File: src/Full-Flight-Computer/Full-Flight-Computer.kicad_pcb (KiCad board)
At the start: 4 copper layers, 93.7 x 43.7 mm, 113 parts, among them J1 Jumper_NO, J2 Jumper_NO, P1 647676-2, P10 Micro_SD_Card, P2 1546551-2, P3 3220-20-0200-00, P4 440054-3, P5 440054-3, P6 440054-3, P7 440054-3, P8 USB, P9 1984659, Q1 QS5U17TR, Q2 QS5U17TR, Q3 QS5U17TR, Q4 QS5U17TR, Q5 QS5U17TR, Q6 QS5U17TR, U1 STM32H750VBTx, U10 TS391IYLT, U11 TS391IYLT, U12 BMM150, U2 LMS8117AMP-3.3_NOPB, U3 BMI323, U4 MAX-8C-0-10, U5 BMP390, U6 SST25VF040B-50-4I-S2AE-T, U7 RFM95W-868S2, U8 CP2102-GMR(QFN28), U9 TS391IYLT, Y1 ECS-240-18-33-JGN-TR

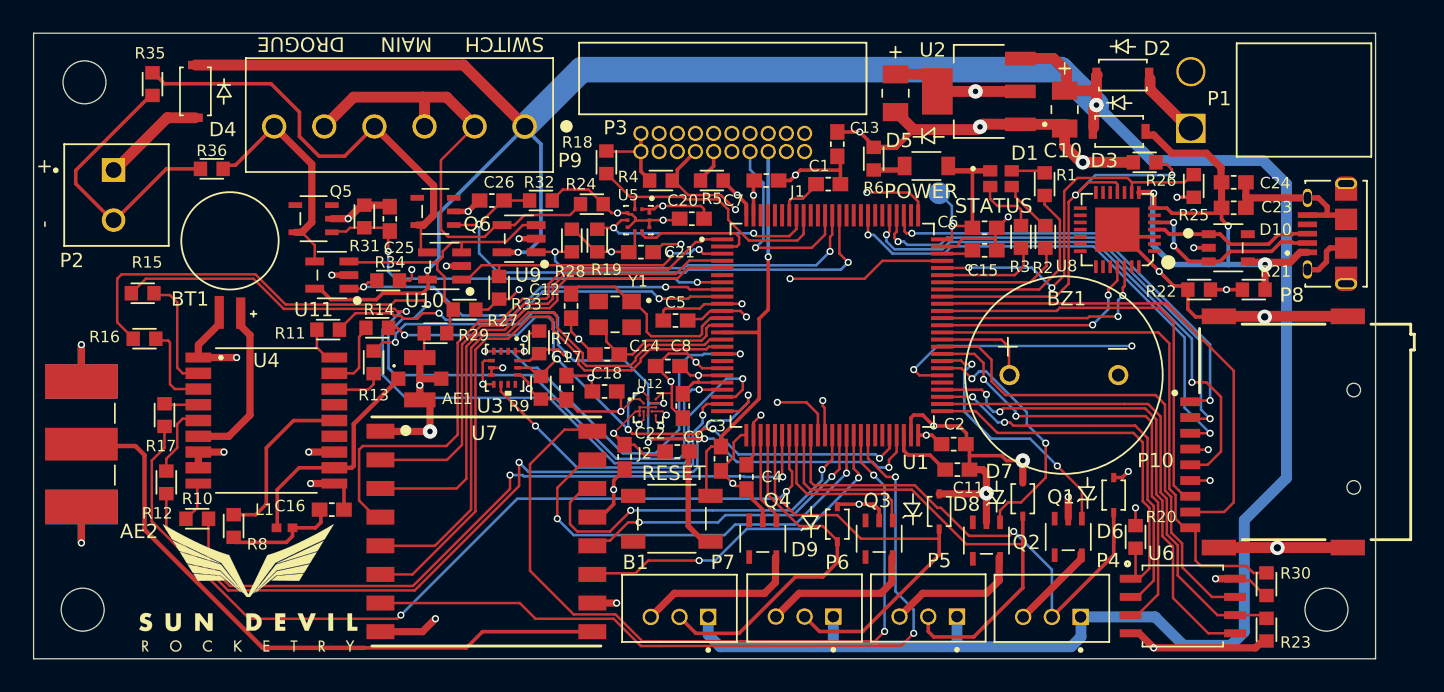
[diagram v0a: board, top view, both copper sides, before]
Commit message: placed all components on test board
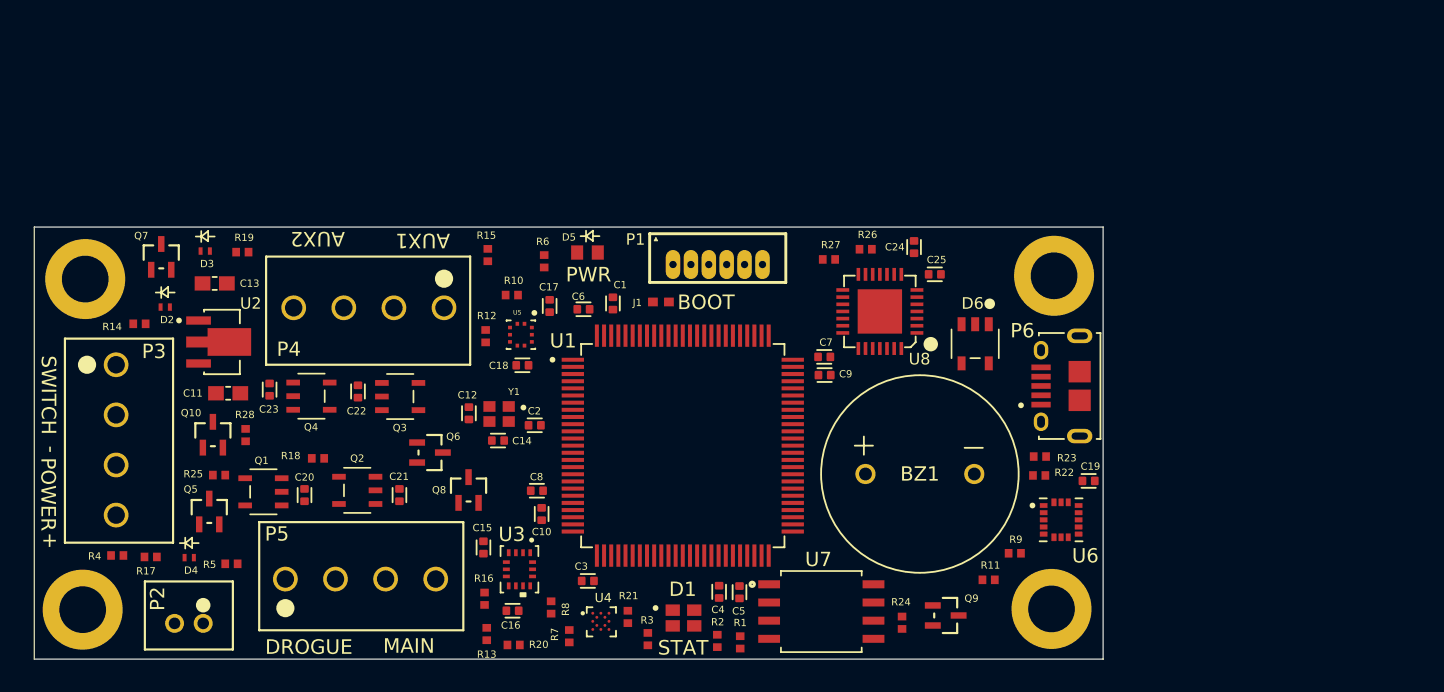
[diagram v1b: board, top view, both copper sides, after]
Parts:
- removed AE1: 0734120110, Flight-Computer:73412-0110
- removed AE2: 142-0701-851, Flight-Computer:142-0701-851
- removed B1: PTS647SM38SMTR2LFS, Flight-Computer:PTS647SM38SMTR2LFS
- removed BT1: MS614SE-FL28E, Flight-Computer:MS621FE-FL11E
- removed the C10 at (165.0, 63.2)
- removed the C16 at (113.8, 91.2)
- removed the C25 at (117.8, 70.9)
- removed C26: 1uF, Flight-Computer:CAP_0603
- removed the C3 at (141.0, 87.6)
- removed the D6 at (168.4, 90.2)
- removed D7, D8, D9: MM3Z3V3B, Flight-Computer:MM3Z3V3B
- removed the H3 at (183.3, 98.2)
- removed J2: Jumper_NO, Engine-Controller:Jumper-NO
- removed L1: 27nH, Flight-Computer:L-07C27NJV6T
- removed LOGO1: Logo, Flight-Computer:Logo
- removed P10: Micro_SD_Card, Flight-Computer:MEM2075-00-140-01-A
- removed the P6 at (148.8, 98.7)
- removed P7: 440054-3, Flight-Computer:440054-3
- removed P9: 1984659, Flight-Computer:1984659
- removed the R10 at (104.4, 91.8)
- removed the R12 at (102.2, 89.3)
- removed the R24 at (132.0, 69.8)
- removed the R27 at (123.1, 77.2)
- removed R29, R30, R33, R34, R35, R36: 10k, Flight-Computer:RES_0603
- removed R31, R32: 100k, Flight-Computer:RES_0603
- removed the R8 at (106.9, 92.3)
- removed TP1: TP, Flight-Computer:TP
- removed U10, U11, U9: TS391IYLT, Flight-Computer:TS391IYLT
- removed the U4 at (109.2, 85.0)
- removed the U7 at (124.6, 92.7)
- added C11: 1uF, Full-Flight-Computer:CAP_0603, F.Cu at (106.6, 83.1)
- added C19: 0.1uF, Full-Flight-Computer:CAP_0402, F.Cu at (166.6, 89.2)
- added C20: 1uF, Full-Flight-Computer:CAP_0402, F.Cu at (111.9, 90.2)
- added C21: 1uF, Full-Flight-Computer:CAP_0402, F.Cu at (118.5, 90.2)
- added C23: 1uF, Full-Flight-Computer:CAP_0402, F.Cu at (109.4, 82.8)
- added H2: Mounting-Hole-4-40, Full-Flight-Computer:MountingHole_4-40, F.Cu at (164.2, 74.9)
- added H4: Mounting-Hole, Full-Flight-Computer:MountingHole_4-40, F.Cu at (96.6, 75.1)
- added Q10: 2N7002W-7-F, Full-Flight-Computer:2N7002W-7-F, F.Cu at (105.5, 86.0)
- added Q7: 2N7002W-7-F, Full-Flight-Computer:2N7002W-7-F, F.Cu at (101.9, 73.5)
- added Q8: 2N7002W-7-F, Full-Flight-Computer:2N7002W-7-F, F.Cu at (123.3, 89.8)
- added Q9: 2N7002W-7-F, Full-Flight-Computer:2N7002W-7-F, F.Cu at (156.7, 98.6)
- added R18: 10k, Full-Flight-Computer:RES_0402, F.Cu at (112.8, 87.6)
- added R19: 10k, Full-Flight-Computer:RES_0402, F.Cu at (107.5, 73.2)
- added R20: 10k, Full-Flight-Computer:RES_0402, F.Cu at (126.5, 100.6)
- added R25: 100k, Full-Flight-Computer:RES_0402, F.Cu at (105.9, 88.8)
- added R9: 10k, Full-Flight-Computer:RES_0402, F.Cu at (161.5, 94.2)
- added U6: H3LIS100DLTR, Full-Flight-Computer:H3LIS100DLTR, F.Cu at (164.7, 91.9)
- BZ1: footprint Flight-Computer:AT-1438-TWT-R -> Full-Flight-Computer:AT-1438-TWT-R
- C1, C12, C14, C2, C5, C6, C7, C8: footprint Flight-Computer:CAP_0603 -> Full-Flight-Computer:CAP_0402
- C10: renamed from C9; footprint Flight-Computer:CAP_0603 -> Full-Flight-Computer:CAP_0402
- C13: value 10uF -> 1uF; footprint Flight-Computer:T491A106K010AT -> Full-Flight-Computer:CAP_0603
- C15: renamed from C17; footprint Flight-Computer:CAP_0603 -> Full-Flight-Computer:CAP_0402
- C16: renamed from C18; footprint Flight-Computer:CAP_0603 -> Full-Flight-Computer:CAP_0402
- C17: renamed from C20; footprint Flight-Computer:CAP_0603 -> Full-Flight-Computer:CAP_0402
- C18: renamed from C21; footprint Flight-Computer:CAP_0603 -> Full-Flight-Computer:CAP_0402
- C22: value 0.1uF -> 1uF; footprint Flight-Computer:CAP_0603 -> Full-Flight-Computer:CAP_0402
- C24: renamed from C23; footprint Flight-Computer:CAP_0603 -> Full-Flight-Computer:CAP_0402
- C25: renamed from C24; footprint Flight-Computer:CAP_0603 -> Full-Flight-Computer:CAP_0402
- C3: renamed from C4; footprint Flight-Computer:CAP_0603 -> Full-Flight-Computer:CAP_0402
- C4: renamed from C11; footprint Flight-Computer:CAP_0603 -> Full-Flight-Computer:CAP_0402
- C9: renamed from C15; footprint Flight-Computer:CAP_0603 -> Full-Flight-Computer:CAP_0402
- D1: footprint Flight-Computer:CLMVC-FKA-CL1D1L71BB7C3C3 -> Full-Flight-Computer:CLMVC-FKA-CL1D1L71BB7C3C3
- D2, D3, D4: value SM5819PL-TP -> PMEG3010AESBYL; footprint Flight-Computer:SM5819PL-TP -> Full-Flight-Computer:PMEG3010AESBYL
- D5: value SML-LX1206GC-TR -> LTST-C191KGKT; footprint Flight-Computer:SML-LX1206GC-TR -> Full-Flight-Computer:LTST-C191KGKT
- D6: renamed from D10; footprint Flight-Computer:SP0504BAHTG -> Full-Flight-Computer:SP0504BAHTG
- H1: value Mounting-Hole -> Mounting-Hole-4-40; footprint Flight-Computer:MountingHole_3mm -> Full-Flight-Computer:MountingHole_4-40
- H3: renamed from H2; footprint Flight-Computer:MountingHole_3mm -> Full-Flight-Computer:MountingHole_4-40
- J1: footprint Flight-Computer:Jumper-NO -> Full-Flight-Computer:Jumper-NO
- P1: value 647676-2 -> 0530470610; footprint Flight-Computer:647676-2 -> Full-Flight-Computer:53047-0610
- P2: value 1546551-2 -> B2B-PH-K-SLFSN_JST; footprint Flight-Computer:1546551-2 -> Full-Flight-Computer:B2B-PH-K-SLFSN_JST
- P3: value 3220-20-0200-00 -> 1984659; footprint Flight-Computer:3220-20-0200-00 -> Full-Flight-Computer:1546551-4
- P4: value 440054-3 -> 1546551-4; footprint Flight-Computer:440054-3 -> Full-Flight-Computer:1546551-4
- P5: value 440054-3 -> 1984659; footprint Flight-Computer:440054-3 -> Full-Flight-Computer:1546551-4
- P6: renamed from P8; footprint Flight-Computer:10118194-0001LF -> Full-Flight-Computer:10118194-0001LF
- Q1, Q2, Q3, Q4: footprint Flight-Computer:QS5U17TR -> Full-Flight-Computer:QS5U17TR
- Q5, Q6: value QS5U17TR -> 2N7002W-7-F; footprint Flight-Computer:QS5U17TR -> Full-Flight-Computer:2N7002W-7-F
- R1: value 68 -> 82; footprint Flight-Computer:RES_0603 -> Full-Flight-Computer:RES_0402
- R10: renamed from R18; footprint Flight-Computer:RES_0603 -> Full-Flight-Computer:RES_0402
- R11, R17: value 33 -> 10k; footprint Flight-Computer:RES_0603 -> Full-Flight-Computer:RES_0402
- R12: renamed from R19; footprint Flight-Computer:RES_0603 -> Full-Flight-Computer:RES_0402
- R13, R14, R15, R16: value 33 -> 100k; footprint Flight-Computer:RES_0603 -> Full-Flight-Computer:RES_0402
- R2, R28, R6: footprint Flight-Computer:RES_0603 -> Full-Flight-Computer:RES_0402
- R21: renamed from R20; footprint Flight-Computer:RES_0603 -> Full-Flight-Computer:RES_0402
- R22: renamed from R21; value 10k -> 100k; footprint Flight-Computer:RES_0603 -> Full-Flight-Computer:RES_0402
- R23: renamed from R22; value 20k -> 200k; footprint Flight-Computer:RES_0603 -> Full-Flight-Computer:RES_0402
- R24: renamed from R23; footprint Flight-Computer:RES_0603 -> Full-Flight-Computer:RES_0402
- R26: renamed from R25; footprint Flight-Computer:RES_0603 -> Full-Flight-Computer:RES_0402
- R27: renamed from R26; footprint Flight-Computer:RES_0603 -> Full-Flight-Computer:RES_0402
- R3: value 280 -> 240; footprint Flight-Computer:RES_0603 -> Full-Flight-Computer:RES_0402
- R4: value 100k -> 39k; footprint Flight-Computer:RES_0603 -> Full-Flight-Computer:RES_0402
- R5: value 100k -> 10k; footprint Flight-Computer:RES_0603 -> Full-Flight-Computer:RES_0402
- R7: footprint Engine-Controller:RES_0603 -> Full-Flight-Computer:RES_0402
- R8: renamed from R9; footprint Engine-Controller:RES_0603 -> Full-Flight-Computer:RES_0402
- U1: footprint Flight-Computer:STM32H750VBT6 -> Full-Flight-Computer:STM32H750VBT6
- U2: value LMS8117AMP-3.3_NOPB -> AP7370-33Y-13; footprint Flight-Computer:LMS8117AMP-3.3NOPB -> Full-Flight-Computer:AP7370-33Y-13
- U3: footprint Flight-Computer:BMI323 -> Full-Flight-Computer:BMI323
- U4: renamed from U12; footprint Flight-Computer:BMM150 -> Full-Flight-Computer:BMM150
- U5: footprint Flight-Computer:BMP390 -> Full-Flight-Computer:BMP390
- U7: renamed from U6; footprint Flight-Computer:SST25VF040B-50-4I-S2AE-T -> Full-Flight-Computer:SST25VF040B-50-4I-S2AE-T
- U8: footprint Flight-Computer:CP2012-GMR -> Full-Flight-Computer:CP2012-GMR
- Y1: footprint Flight-Computer:ECS-240-18-33-JGN-TR -> Full-Flight-Computer:ECS-240-12-37B-CKY-TR
- moved H1 76.9 mm to (164.1, 98.1)
- moved D2 68.8 mm to (102.2, 77.0)
- moved D3 64.4 mm to (105.0, 73.1)
- moved Q1 56.3 mm to (109.0, 89.9), turned to 180 degrees
- moved U2 55.7 mm to (106.1, 79.5), turned to 0 degrees
- moved P4 49.4 mm to (121.6, 77.1)
- moved C13 49.4 mm to (105.6, 75.4), turned to 0 degrees
- moved R11 49.3 mm to (159.7, 96.1), turned to 0 degrees
- moved P5 47.0 mm to (110.5, 96.0), turned to 0 degrees
- moved R4 46.1 mm to (98.8, 94.4), turned to 0 degrees
- moved P3 45.3 mm to (98.7, 81.1), turned to -90 degrees
- moved Q2 44.1 mm to (115.6, 89.8), turned to 180 degrees
- moved R5 42.9 mm to (106.8, 95.0)
- moved R1 38.4 mm to (142.3, 100.5)
- moved R3 38.3 mm to (135.9, 100.2), turned to -90 degrees
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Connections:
- BZ1 pad 1: BEEP -> VIN
- BZ1 pad 2: Earth -> Net-(BZ1-+)
- C22 pad 1: 3.3V -> AUX1
- P1 pad 1: /PIN_HARN -> 3.3V
- P1 pad 2: Earth -> SWDIO
- P2 pad 1: /PIN_SCREW -> Earth
- P2 pad 2: Earth -> Net-(P2-6)
- P3 pad 1: 3.3V -> VIN
- P3 pad 2: 3.3V -> VIN_SW
- P3 pad 4: Earth -> Net-(P3B-6)
- P4 pad 1: VIN -> VIN_SW
- P4 pad 2: MOTOR1_PWM -> Net-(P4A-6)
- P4 pad 3: Net-(P4-Pad3) -> VIN_SW
- P5 pad 1: VIN -> VIN_SW
- P5 pad 2: MOTOR3_PWM -> Net-(P5A-6)
- P5 pad 3: Net-(P5-Pad3) -> VIN_SW
- Q1 pad 1: MOTOR1_EN -> DROGUE
- Q1 pad 5: Net-(P4-Pad3) -> Net-(P5A-6)
- Q2 pad 1: MOTOR3_EN -> MAIN
- Q2 pad 5: Net-(P5-Pad3) -> Net-(P5B-6)
- Q3 pad 1: MOTOR2_EN -> AUX1
- Q3 pad 5: Net-(P6-Pad3) -> Net-(P4A-6)
- Q4 pad 1: MOTOR4_EN -> AUX2
- Q4 pad 5: Net-(P7-Pad3) -> Net-(P4B-6)
- Q5 pad 1: DROGUE -> Net-(P5B-6)
- Q5 pad 3: unconnected-(Q5-Pad3) -> ~{MAIN_CONT}
- Q6 pad 1: MAIN -> Net-(P4A-6)
- Q6 pad 3: unconnected-(Q6-Pad3) -> ~{AUX1_CONT}
- R11 pad 1: ~{GPS_SBOOT} -> HG_ACC_SDA
- R11 pad 2: Net-(R11-Pad2) -> 3.3V
- R13 pad 1: SDA -> Earth
- R13 pad 2: Net-(R13-Pad2) -> Net-(P5B-6)
- R14 pad 1: SCL -> Earth
- R14 pad 2: Net-(R14-Pad2) -> Net-(P4A-6)
- R15 pad 1: Net-(R15-Pad1) -> Earth
- R15 pad 2: GPS_TX -> Net-(P4B-6)
- R16 pad 1: Net-(R16-Pad1) -> Earth
- R16 pad 2: GPS_RX -> Net-(P5A-6)
- R17 pad 1: Net-(R17-Pad1) -> ~{MAIN_CONT}
- R17 pad 2: GPS_TIM -> 3.3V
- R4 pad 1: SWDIO -> VIN
- R4 pad 2: 3.3V -> VBAT_SENSE
- R5 pad 1: SWCLK -> Earth
- R5 pad 2: 3.3V -> VBAT_SENSE
- U1 pad 1: W_SCK -> unconnected-(U1-PE2-Pad1)
- U1 pad 15: W_SS -> unconnected-(U1-PC0-Pad15)
- U1 pad 16: W_RST -> unconnected-(U1-PC1-Pad16)
- U1 pad 22: GPS_RX -> unconnected-(U1-PA0-Pad22)
- U1 pad 23: GPS_TX -> unconnected-(U1-PA1-Pad23)
- U1 pad 25: GPS_INT -> unconnected-(U1-PA3-Pad25)
- U1 pad 28: MOTOR4_EN -> unconnected-(U1-PA4-Pad28)
- U1 pad 29: MOTOR4_PWM -> unconnected-(U1-PA5-Pad29)
- U1 pad 30: MOTOR2_PWM -> VBAT_SENSE
- U1 pad 31: ~{GPS_RST} -> unconnected-(U1-PA7-Pad31)
- U1 pad 32: GPS_TIM -> unconnected-(U1-PC4-Pad32)
- U1 pad 33: MOTOR2_EN -> unconnected-(U1-PC5-Pad33)
- U1 pad 34: MOTOR3_PWM -> HG_ACC_INT1
- U1 pad 35: MOTOR1_PWM -> HG_ACC_INT2
- U1 pad 38: W_IO0 -> unconnected-(U1-PE8-Pad38)
- U1 pad 39: W_IO4 -> unconnected-(U1-PE9-Pad39)
- U1 pad 4: W_MISO -> unconnected-(U1-PE5-Pad4)
- U1 pad 40: W_IO1 -> unconnected-(U1-PE10-Pad40)
- U1 pad 41: W_IO3 -> unconnected-(U1-PE11-Pad41)
- U1 pad 42: W_IO2 -> AUX1
- U1 pad 43: W_IO5 -> AUX2
- U1 pad 44: unconnected-(U1-Pad44) -> ~{AUX1_CONT}
- U1 pad 45: unconnected-(U1-Pad45) -> ~{AUX2_CONT}
- U1 pad 5: W_MOSI -> unconnected-(U1-PE6-Pad5)
- U1 pad 57: MOTOR3_EN -> unconnected-(U1-PD10-Pad57)
- U1 pad 58: MOTOR1_EN -> unconnected-(U1-PD11-Pad58)
- U1 pad 62: ~{SD_DETECT} -> unconnected-(U1-PD15-Pad62)
- U1 pad 65: SD_DAT0 -> unconnected-(U1-PC8-Pad65)
- U1 pad 66: SD_DAT1 -> unconnected-(U1-PC9-Pad66)
- U1 pad 78: SD_DAT2 -> unconnected-(U1-PC10-Pad78)
- U1 pad 79: SD_DAT3 -> unconnected-(U1-PC11-Pad79)
- U1 pad 80: SD_CLK -> unconnected-(U1-PC12-Pad80)
- U1 pad 83: SD_CMD -> unconnected-(U1-PD2-Pad83)
- U1 pad 9: ~{GPS_SBOOT} -> unconnected-(U1-PC15-Pad9)
- U1 pad 95: unconnected-(U1-Pad95) -> HG_ACC_SCL
- U1 pad 96: unconnected-(U1-Pad96) -> HG_ACC_SDA
- U2 pad 1: Earth -> 3.3V
- U2 pad 2: 3.3V -> Earth
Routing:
- net Earth: track 236.5 -> 0.00 mm, vias 43 -> 0
- net VIN: track 206.8 -> 0.00 mm, vias 3 -> 0
- net 3.3V: track 94.3 -> 0.00 mm, vias 23 -> 0
- net GPS_RX: track 64.1 -> 0.00 mm, vias 2 -> 0
- net GPS_TIM: track 62.0 -> 0.00 mm, vias 2 -> 0
- net GPS_TX: track 60.2 -> 0.00 mm, vias 2 -> 0
- net GPS_INT: track 56.3 -> 0.00 mm, vias 2 -> 0
- net W_IO5: track 54.4 -> 0.00 mm, vias 2 -> 0
- net W_IO2: track 54.2 -> 0.00 mm, vias 2 -> 0
- net SDA: track 53.1 -> 0.00 mm, vias 6 -> 0
- net ~{GPS_RST}: track 50.7 -> 0.00 mm, vias 2 -> 0
- net SCL: track 49.8 -> 0.00 mm, vias 6 -> 0
- net Net-(AE2-Pad1): track 43.2 -> 0.00 mm
- net W_SCK: track 41.2 -> 0.00 mm
- net W_RST: track 41.1 -> 0.00 mm
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- removed copper zone on In2.Cu, net 3.3V
- removed copper zone on In1.Cu, net Earth
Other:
- board size 93.7 x 43.7 mm -> 74.7 x 30.2 mm
- board text added: "A0002 Rev 2.0 Full-Feature Flight Computer Test Board"
- board text added: "AUX1"
- board text added: "AUX2"
- board text added: "BOOT"
- board text added: "PWR"
- board text added: "STAT"
- board text removed: "A0002 Flight Computer Rev 2.0"
- board text removed: "RESET"
- board text removed: "STATUS"

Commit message: completed initial layout
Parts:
- moved R4 64.7 mm to (159.7, 72.4), turned to 180 degrees
- moved D3 55.1 mm to (160.0, 75.3)
- moved R5 55.1 mm to (157.0, 72.4)
- moved R20 28.7 mm to (98.5, 94.4)
- moved R16 23.7 mm to (100.9, 94.6), turned to 0 degrees
- moved R17 21.4 mm to (122.3, 91.0)
- moved R21 20.9 mm to (155.3, 99.0)
- moved Q5 19.9 mm to (125.1, 91.7)
- moved Q8 18.4 mm to (105.0, 91.7), turned to 90 degrees
- moved D2 18.2 mm to (107.3, 94.5)
- moved R15 18.1 mm to (106.6, 73.4), turned to 0 degrees
- moved R14 16.9 mm to (115.6, 85.5), turned to 180 degrees
- moved R18 9.31 mm to (121.6, 84.4), turned to 90 degrees
- moved R19 7.43 mm to (101.2, 77.1)
- moved R7 5.80 mm to (129.3, 94.3), turned to 0 degrees
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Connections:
- U1 pad 15: unconnected-(U1-PC0-Pad15) -> ~{AUX1_CONT}
- U1 pad 16: unconnected-(U1-PC1-Pad16) -> MAIN
- U1 pad 17: IMU_INT1 -> DROGUE
- U1 pad 18: unconnected-(U1-PC3_C-Pad18) -> ~{DROGUE_CONT}
- U1 pad 22: unconnected-(U1-PA0-Pad22) -> ~{MAIN_CONT}
- U1 pad 24: IMU_INT2 -> IMU_INT1
- U1 pad 25: unconnected-(U1-PA3-Pad25) -> IMU_INT2
- U1 pad 3: ~{MAIN_CONT} -> unconnected-(U1-PE4-Pad3)
- U1 pad 31: unconnected-(U1-PA7-Pad31) -> MAG_DRDY
- U1 pad 32: unconnected-(U1-PC4-Pad32) -> MAG_INT
- U1 pad 34: HG_ACC_INT1 -> unconnected-(U1-PB0-Pad34)
- U1 pad 35: HG_ACC_INT2 -> unconnected-(U1-PB1-Pad35)
- U1 pad 36: MAG_DRDY -> unconnected-(U1-PB2-Pad36)
- U1 pad 37: MAG_INT -> unconnected-(U1-PE7-Pad37)
- U1 pad 39: unconnected-(U1-PE9-Pad39) -> STATUS_R
- U1 pad 41: unconnected-(U1-PE11-Pad41) -> STATUS_B
- U1 pad 42: AUX1 -> unconnected-(U1-PE12-Pad42)
- U1 pad 43: AUX2 -> STATUS_G
- U1 pad 44: ~{AUX1_CONT} -> unconnected-(U1-PE14-Pad44)
- U1 pad 45: ~{AUX2_CONT} -> unconnected-(U1-PE15-Pad45)
- U1 pad 5: unconnected-(U1-PE6-Pad5) -> ~{AUX2_CONT}
- U1 pad 55: unconnected-(U1-PD8-Pad55) -> HG_ACC_INT1
- U1 pad 56: USB_DETECT -> HG_ACC_INT2
- U1 pad 57: unconnected-(U1-PD10-Pad57) -> USB_DETECT
- U1 pad 68: STATUS_B -> unconnected-(U1-PA9-Pad68)
- U1 pad 69: STATUS_G -> unconnected-(U1-PA10-Pad69)
- U1 pad 7: DROGUE -> AUX2
- U1 pad 70: STATUS_R -> unconnected-(U1-PA11-Pad70)
- U1 pad 8: ~{DROGUE_CONT} -> AUX1
- U1 pad 87: MAIN -> unconnected-(U1-PD6-Pad87)
- U1 pad 88: ~{SWITCH} -> unconnected-(U1-PD7-Pad88)
- U1 pad 9: unconnected-(U1-PC15-Pad9) -> ~{SWITCH}
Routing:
- net Earth: track 0.00 -> 140.1 mm, vias 0 -> 33
- net VIN: track 0.00 -> 123.9 mm, vias 0 -> 3
- net 3.3V: track 0.00 -> 102.7 mm, vias 0 -> 22
- net VIN_SW: track 0.00 -> 67.4 mm
- net VBAT_SENSE: track 0.00 -> 47.2 mm, vias 0 -> 2
- net HG_ACC_SCL: track 0.00 -> 46.8 mm, vias 0 -> 3
- net ~{DROGUE_CONT}: track 0.00 -> 42.4 mm
- net ~{AUX2_CONT}: track 0.00 -> 41.6 mm, vias 0 -> 2
- net HG_ACC_SDA: track 0.00 -> 39.8 mm, vias 0 -> 2
- net 5V: track 0.00 -> 37.1 mm, vias 0 -> 1
- net SDA: track 0.00 -> 32.6 mm, vias 0 -> 2
- net AUX2: track 0.00 -> 31.9 mm
- net ~{SWITCH}: track 0.00 -> 29.8 mm
- net Net-(P5A-6): track 0.00 -> 29.3 mm
- net ~{FLASH_SS}: track 0.00 -> 24.3 mm, vias 0 -> 2
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- added copper zone on In2.Cu, net 3.3V
- added copper zone on B.Cu, net Earth
- added copper zone on F.Cu, net Earth
- added copper zone on In1.Cu, net Earth

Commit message: resolved all DRC errors
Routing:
- net Earth: track 140.1 -> 146.5 mm
- net 5V: track 37.1 -> 35.6 mm, vias 1 -> 0
- net HG_ACC_SCL: vias 3 -> 2
- removed copper zone on F.Cu, net Earth

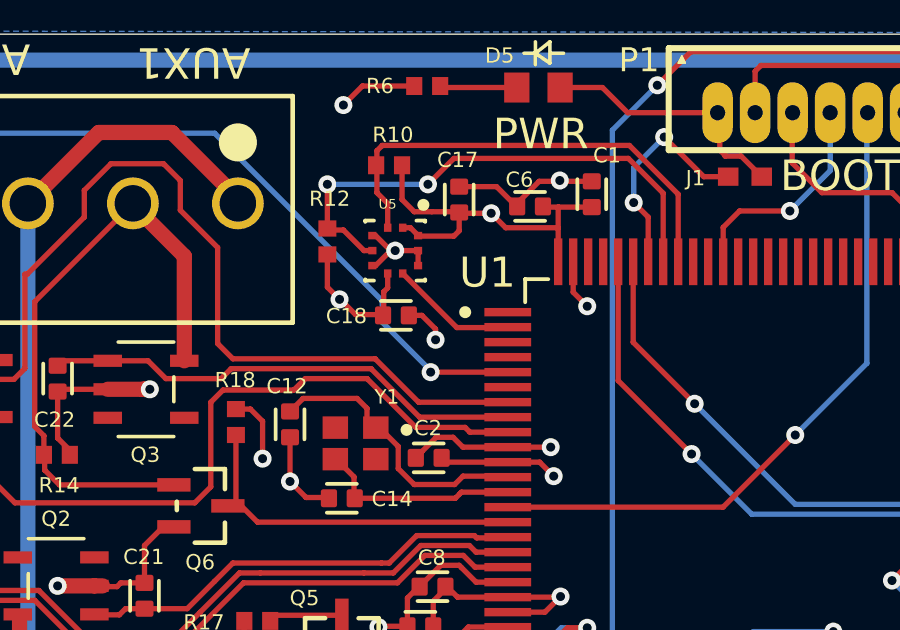
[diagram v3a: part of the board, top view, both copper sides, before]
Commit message: moved BP_INT signal to new MCU pin to avoid EXTI collision with IMU interrupt signal
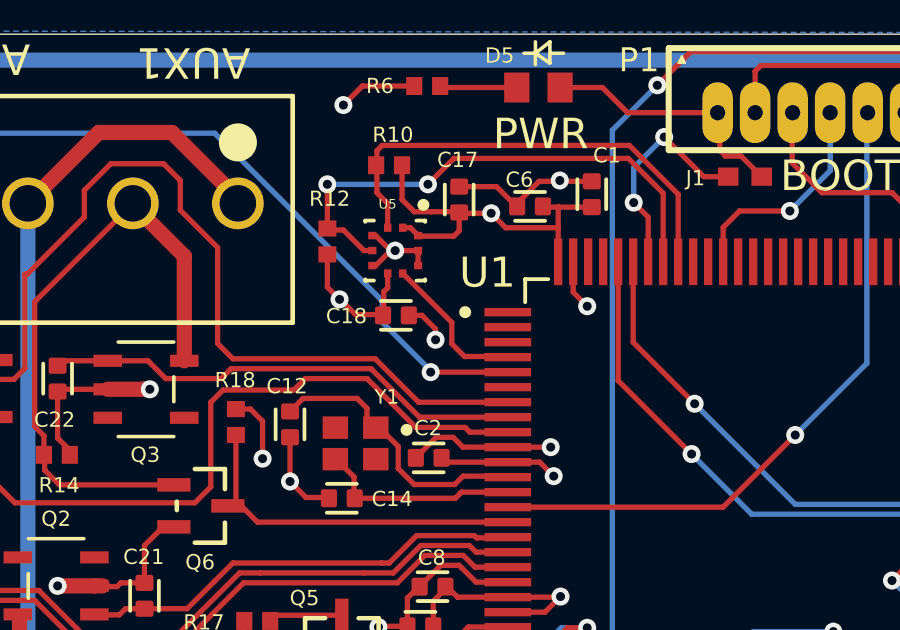
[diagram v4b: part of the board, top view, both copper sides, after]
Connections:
- U1 pad 2: BP_INT -> unconnected-(U1-PE3-Pad2)
- U1 pad 4: unconnected-(U1-PE5-Pad4) -> BP_INT
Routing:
- net BP_INT: track 3.90 -> 4.51 mm
